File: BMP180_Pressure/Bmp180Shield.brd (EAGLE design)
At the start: 39.7 x 26.7 mm, 5 parts

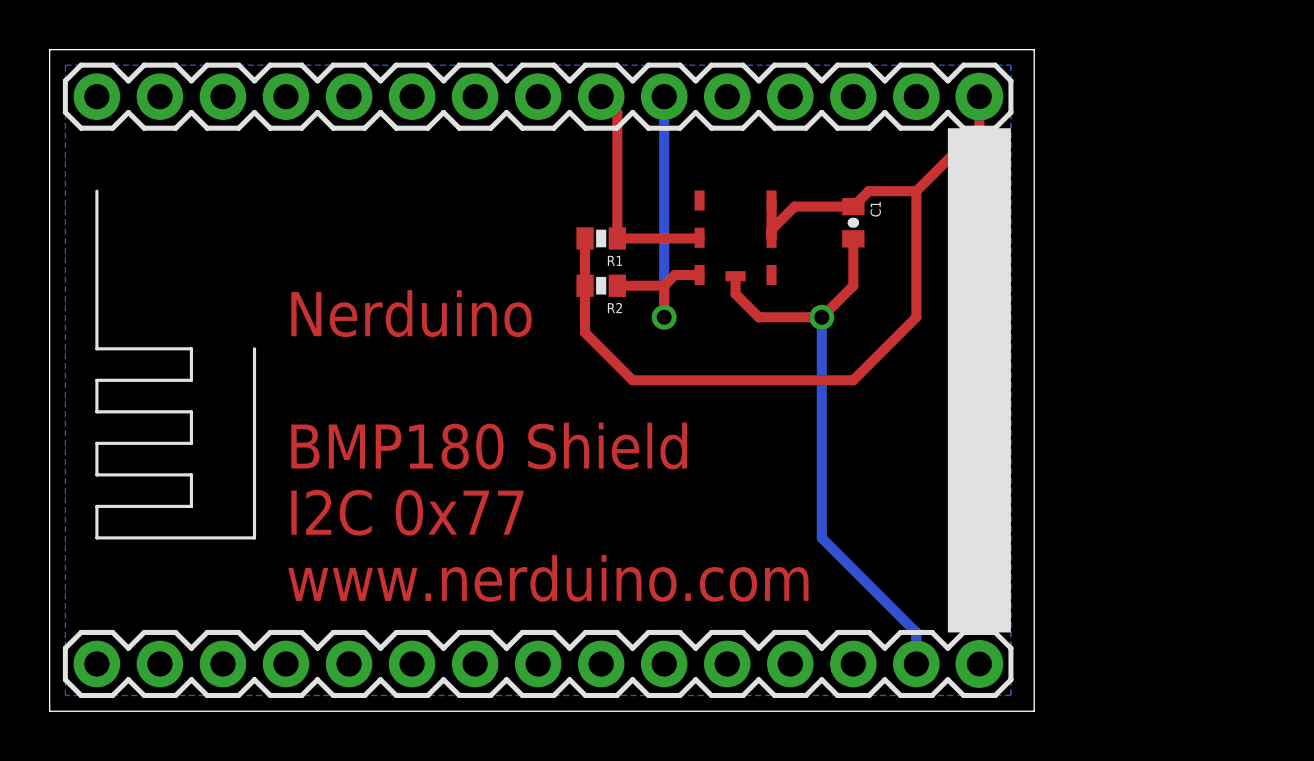
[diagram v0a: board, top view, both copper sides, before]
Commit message: Updated stencil text Added PCA9685 and ITG3200 shields
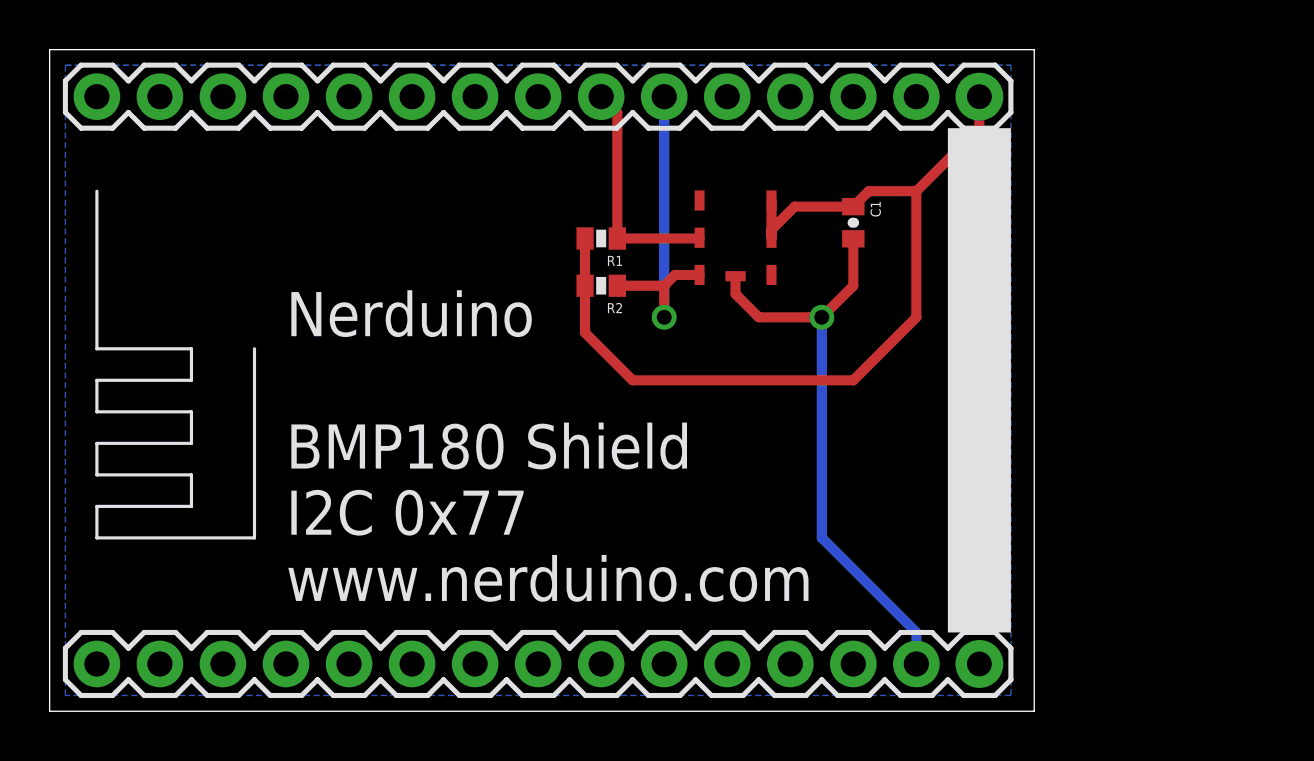
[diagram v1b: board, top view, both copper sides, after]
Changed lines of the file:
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@@
 <wire x1="39.04" y1="26.025" x2="-0.635" y2="26.025" width="0" layer="20"/>
 <wire x1="-0.635" y1="26.025" x2="-0.635" y2="-0.635" width="0" layer="20"/>
-<text x="8.89" y="3.81" size="1.778" layer="1">Nerduino
+<text x="8.89" y="3.81" size="1.778" layer="121">Nerduino
 BMP180 Shield
 I2C 0x77

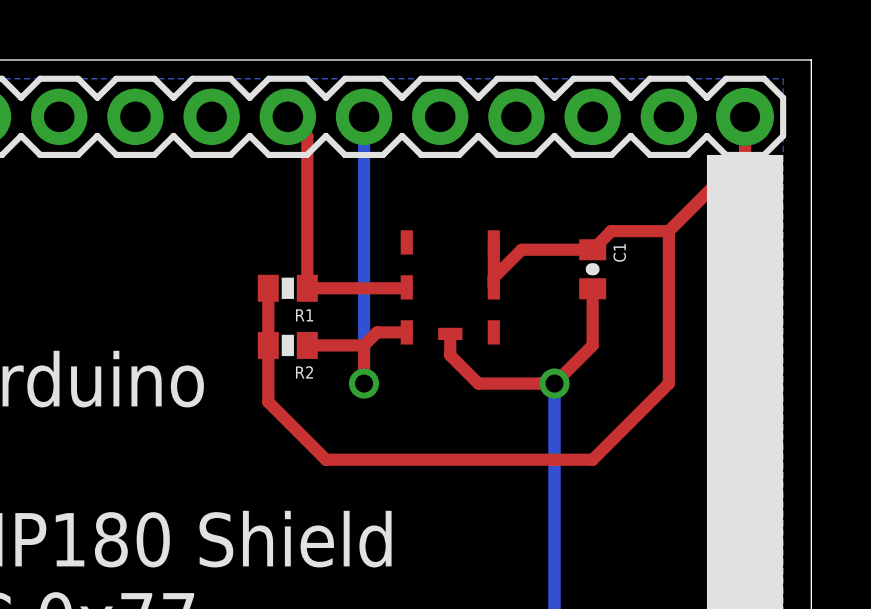
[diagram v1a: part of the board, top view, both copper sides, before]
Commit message: Updated BMP180 symbol Removed BMP085 shield (redundant) Added DS3231 RTC Shield Added LTC2495 ADC Shield Added chip data sheets for each shield
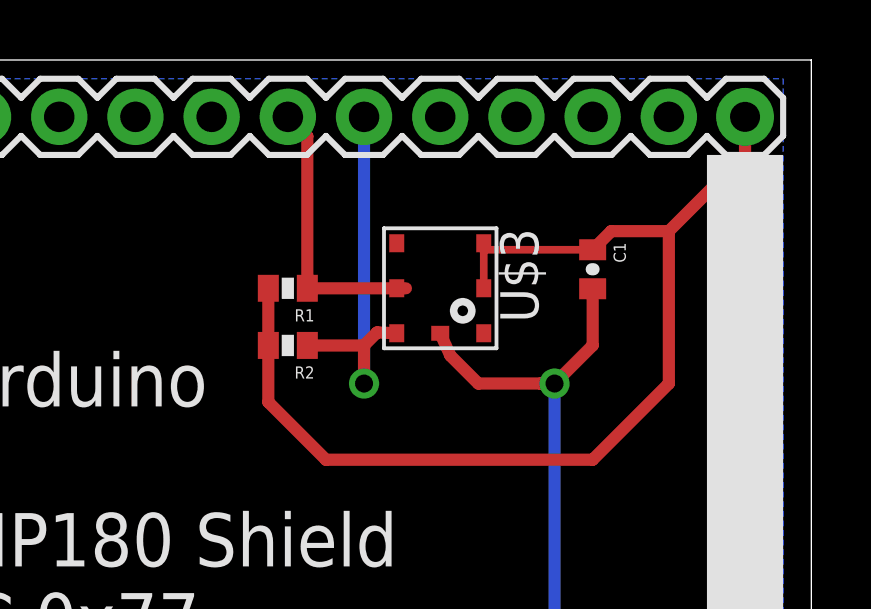
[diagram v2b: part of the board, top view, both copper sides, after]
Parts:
- U$3: device NerduinoShieldLib:BMP180 -> SparkFun-Sensors:BMP180
- moved U$3 1.42 mm to (26.7, 18.4), turned to 270 degrees
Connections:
- net 3.3V: now also U$3.2, U$3.3; no longer U$3.P$2, U$3.P$3
- net GND: now also U$3.7; no longer U$3.P$7
- net N$2: now also U$3.6; no longer U$3.P$6
- net N$3: now also U$3.5; no longer U$3.P$5
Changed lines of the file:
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@@
 <?xml version="1.0" encoding="utf-8"?>
 <!DOCTYPE eagle SYSTEM "eagle.dtd">
-<eagle version="7.3.0">
+<eagle version="7.4.0">
 <drawing>
 <settings>
@@
 <layer number="54" name="bGND_GNDA" color="1" fill="9" visible="no" active="no"/>
 <layer number="56" name="wert" color="7" fill="1" visible="no" active="no"/>
+<layer number="57" name="tCAD" color="7" fill="1" visible="no" active="no"/>
+<layer number="59" name="tCarbon" color="7" fill="1" visible="no" active="no"/>
+<layer number="60" name="bCarbon" color="7" fill="1" visible="no" active="no"/>
 <layer number="90" name="Modules" color="5" fill="1" visible="no" active="no"/>
 <layer number="91" name="Nets" color="2" fill="1" visible="no" active="no"/>
@@
 <layer number="97" name="Info" color="7" fill="1" visible="no" active="no"/>
 <layer number="98" name="Guide" color="6" fill="1" visible="no" active="no"/>
+<layer number="99" name="SpiceOrder" color="7" fill="1" visible="no" active="no"/>
 <layer number="100" name="Muster" color="7" fill="1" visible="no" active="no"/>
 <layer number="101" name="Patch_Top" color="12" fill="4" visible="yes" active="yes"/>
@@
 <layer number="106" name="bPlate" color="7" fill="1" visible="yes" active="yes"/>
 <layer number="107" name="Crop" color="7" fill="1" visible="yes" active="yes"/>
+<layer number="108" name="tplace-old" color="10" fill="1" visible="yes" active="yes"/>
+<layer number="109" name="ref-old" color="11" fill="1" visible="yes" active="yes"/>
+<layer number="110" name="fp0" color="7" fill="1" visible="yes" active="yes"/>
+<layer number="111" name="LPC17xx" color="7" fill="1" visible="yes" active="yes"/>
+<layer number="112" name="tSilk" color="7" fill="1" visible="yes" active="yes"/>
+<layer number="113" name="IDFDebug" color="7" fill="1" visible="yes" active="yes"/>
 <layer number="116" name="Patch_BOT" color="9" fill="4" visible="yes" active="yes"/>
+<layer number="118" name="Rect_Pads" color="7" fill="1" visible="yes" active="yes"/>
 <layer number="121" name="_tsilk" color="7" fill="1" visible="yes" active="yes"/>
 <layer number="122" name="_bsilk" color="7" fill="1" visible="yes" active="yes"/>
+<layer number="123" name="tTestmark" color="7" fill="1" visible="yes" active="yes"/>
+<layer number="124" name="bTestmark" color="7" fill="1" visible="yes" active="yes"/>
 <layer number="125" name="_tNames" color="7" fill="1" visible="yes" active="yes"/>
+<layer number="126" name="_bNames" color="7" fill="1" visible="yes" active="yes"/>
+<layer number="127" name="_tValues" color="7" fill="1" visible="yes" active="yes"/>
+<layer number="128" name="_bValues" color="7" fill="1" visible="yes" active="yes"/>
+<layer number="129" name="Mask" color="7" fill="1" visible="yes" active="yes"/>
+<layer number="131" name="tAdjust" color="7" fill="1" visible="yes" active="yes"/>
+<layer number="132" name="bAdjust" color="7" fill="1" visible="yes" active="yes"/>
 <layer number="144" name="Drill_legend" color="7" fill="1" visible="yes" active="yes"/>
+<layer number="150" name="Notes" color="7" fill="1" visible="yes" active="yes"/>
 <layer number="151" name="HeatSink" color="7" fill="1" visible="yes" active="yes"/>
+<layer number="152" name="_bDocu" color="7" fill="1" visible="yes" active="yes"/>
+<layer number="153" name="FabDoc1" color="7" fill="1" visible="yes" active="yes"/>
+<layer number="154" name="FabDoc2" color="7" fill="1" visible="yes" active="yes"/>
+<layer number="155" name="FabDoc3" color="7" fill="1" visible="yes" active="yes"/>
+<layer number="199" name="Contour" color="7" fill="1" visible="yes" active="yes"/>
 <layer number="200" name="200bmp" color="1" fill="10" visible="yes" active="yes"/>
 <layer number="201" name="201bmp" color="2" fill="10" visible="yes" active="yes"/>
@@
 <layer number="223" name="223bmp" color="24" fill="1" visible="no" active="no"/>
 <layer number="224" name="224bmp" color="25" fill="1" visible="no" active="no"/>
+<layer number="225" name="225bmp" color="7" fill="1" visible="yes" active="yes"/>
+<layer number="226" name="226bmp" color="7" fill="1" visible="yes" active="yes"/>
+<layer number="227" name="227bmp" color="7" fill="1" visible="yes" active="yes"/>
+<layer number="228" name="228bmp" color="7" fill="1" visible="yes" active="yes"/>
+<layer number="229" name="229bmp" color="7" fill="1" visible="yes" active="yes"/>
+<layer number="230" name="230bmp" color="7" fill="1" visible="yes" active="yes"/>
+<layer number="231" name="231bmp" color="7" fill="1" visible="yes" active="yes"/>
+<layer number="248" name="Housing" color="7" fill="1" visible="yes" active="yes"/>
+<layer number="249" name="Edge" color="7" fill="1" visible="yes" active="yes"/>
 <layer number="250" name="Descript" color="3" fill="1" visible="no" active="no"/>
 <layer number="251" name="SMDround" color="12" fill="11" visible="no" active="no"/>
 <layer number="254" name="cooling" color="7" fill="1" visible="yes" active="yes"/>
+<layer number="255" name="routoute" color="7" fill="1" visible="yes" active="yes"/>
 </layers>
 <board>
@@
 <element name="R2" library="SparkFun" package="0402-RES" value="4.7k" x="21.59" y="16.51" rot="R180"/>
 <element name="U$1" library="NerduinoShieldLib" package="NERDUINO_STACK" value="NERDSHIELD" x="19.05" y="6.35"/>
-<element name="U$3" library="NerduinoShieldLib" package="BMP180" value="BMP180" x="27.305" y="17.145" rot="R180"/>
+<element name="U$3" library="SparkFun-Sensors" package="BMP180" value="BMP180" x="26.67" y="18.415" rot="R270"/>
 </elements>
 <signals>
@@
 <wire x1="31.75" y1="16.51" x2="30.48" y2="15.24" width="0.4064" layer="1"/>
 <wire x1="30.48" y1="15.24" x2="30.005" y2="15.24" width="0.4064" layer="1"/>
-<wire x1="29.21" y1="16.51" x2="30.48" y2="15.24" width="0" layer="19" extent="1-16"/>
 <via x="30.48" y="15.24" extent="1-16" drill="0.6" shape="square"/>
 <wire x1="30.48" y1="15.24" x2="30.48" y2="6.35" width="0.4064" layer="16"/>
 <wire x1="30.48" y1="6.35" x2="34.29" y2="2.54" width="0.4064" layer="16"/>
 <wire x1="34.29" y1="2.54" x2="34.29" y2="1.27" width="0.4064" layer="16"/>
-<contactref element="U$3" pad="P$7"/>
-<wire x1="27.005" y1="16.895" x2="27.005" y2="16.175" width="0.4064" layer="1"/>
+<contactref element="U$3" pad="7"/>
+<wire x1="26.67" y1="16.915" x2="27.005" y2="16.175" width="0.4064" layer="1"/>
 <wire x1="27.005" y1="16.175" x2="27.94" y2="15.24" width="0.4064" layer="1"/>
 <wire x1="27.94" y1="15.24" x2="30.48" y2="15.24" width="0.4064" layer="1"/>
@@
 <wire x1="34.29" y1="20.32" x2="32.37" y2="20.32" width="0.4064" layer="1"/>
 <wire x1="32.37" y1="20.32" x2="31.75" y2="19.7" width="0.4064" layer="1"/>
-<wire x1="31.75" y1="19.7" x2="29.385" y2="19.7" width="0.4064" layer="1"/>
 <wire x1="20.94" y1="18.415" x2="20.94" y2="16.51" width="0.4064" layer="1"/>
 <wire x1="20.94" y1="16.51" x2="20.94" y2="14.62" width="0.4064" layer="1"/>
@@
 <wire x1="31.75" y1="12.7" x2="34.29" y2="15.24" width="0.4064" layer="1"/>
 <wire x1="34.29" y1="15.24" x2="34.29" y2="20.32" width="0.4064" layer="1"/>
-<contactref element="U$3" pad="P$2"/>
-<contactref element="U$3" pad="P$3"/>
-<wire x1="28.455" y1="19.945" x2="28.455" y2="18.445" width="0.4064" layer="1"/>
-<wire x1="28.455" y1="18.445" x2="28.455" y2="18.77" width="0.4064" layer="1"/>
-<wire x1="28.455" y1="18.77" x2="29.385" y2="19.7" width="0.4064" layer="1"/>
+<contactref element="U$3" pad="2"/>
+<contactref element="U$3" pad="3"/>
+<wire x1="31.75" y1="19.7" x2="28.12" y2="19.7" width="0.254" layer="1"/>
+<wire x1="28.12" y1="19.7" x2="28.12" y2="19.915" width="0.254" layer="1"/>
+<wire x1="28.12" y1="19.915" x2="28.12" y2="18.415" width="0.254" layer="1"/>
 </signal>
 <signal name="N$2">
@@
 <via x="24.13" y="15.24" extent="1-16" drill="0.6" shape="square"/>
 <wire x1="24.13" y1="15.24" x2="24.13" y2="16.51" width="0.4064" layer="1"/>
-<contactref element="U$3" pad="P$6"/>
-<wire x1="25.555" y1="16.945" x2="24.565" y2="16.945" width="0.4064" layer="1"/>
+<contactref element="U$3" pad="6"/>
+<wire x1="25.22" y1="16.915" x2="24.565" y2="16.945" width="0.4064" layer="1"/>
 <wire x1="24.565" y1="16.945" x2="24.13" y2="16.51" width="0.4064" layer="1"/>
 </signal>
@@
 <wire x1="22.24" y1="18.415" x2="22.24" y2="23.48" width="0.4064" layer="1"/>
 <wire x1="22.24" y1="23.48" x2="21.59" y2="24.13" width="0.4064" layer="1"/>
-<contactref element="U$3" pad="P$5"/>
-<wire x1="22.24" y1="18.415" x2="25.525" y2="18.415" width="0.4064" layer="1"/>
-<wire x1="25.525" y1="18.415" x2="25.555" y2="18.445" width="0.4064" layer="1"/>
+<contactref element="U$3" pad="5"/>
+<wire x1="22.24" y1="18.415" x2="25.22" y2="18.415" width="0.4064" layer="1"/>
+<wire x1="25.525" y1="18.415" x2="25.22" y2="18.415" width="0.4064" layer="1"/>
 </signal>
 </signals>
